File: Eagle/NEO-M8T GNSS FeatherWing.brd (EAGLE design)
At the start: 50.8 x 22.9 mm, 31 parts, among them Q1 DMG3415U-7, Q2 2N2222, SW1 KMR2, U1 NEO-M8, X1 uFL

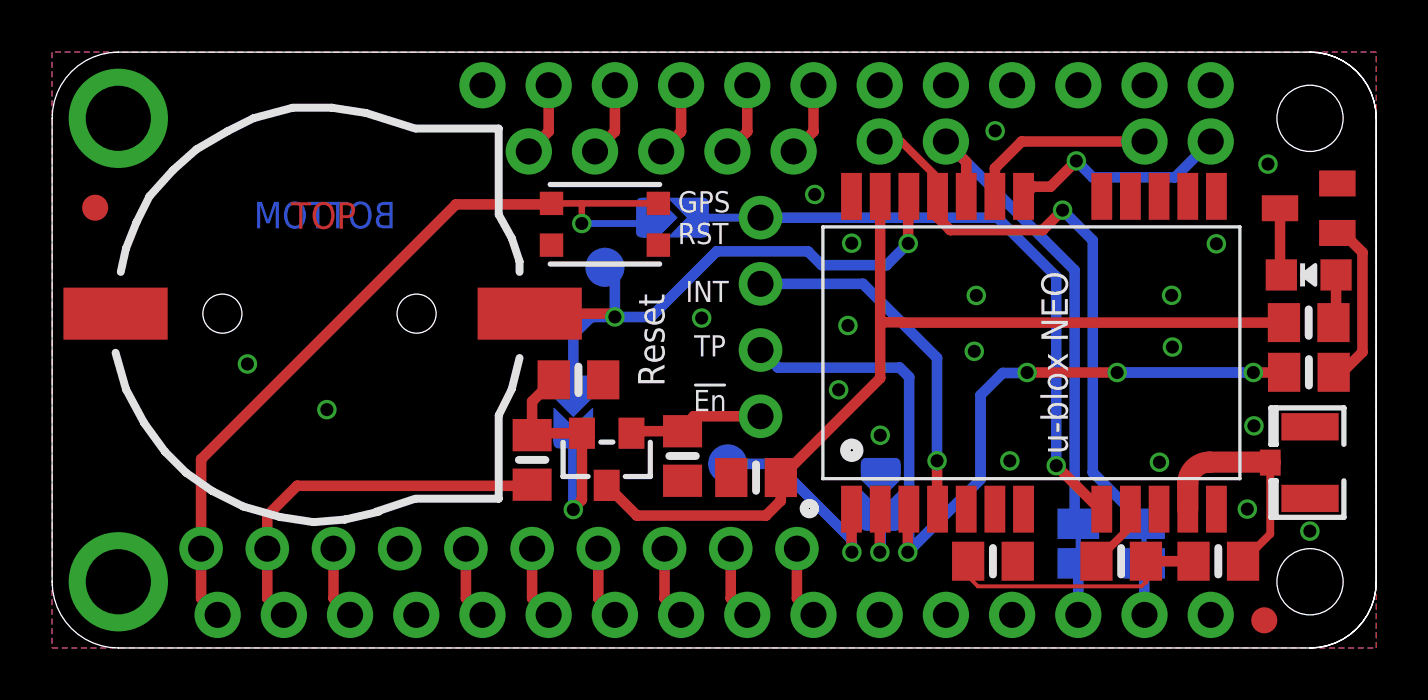
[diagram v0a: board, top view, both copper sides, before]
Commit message: Groundplane improvements
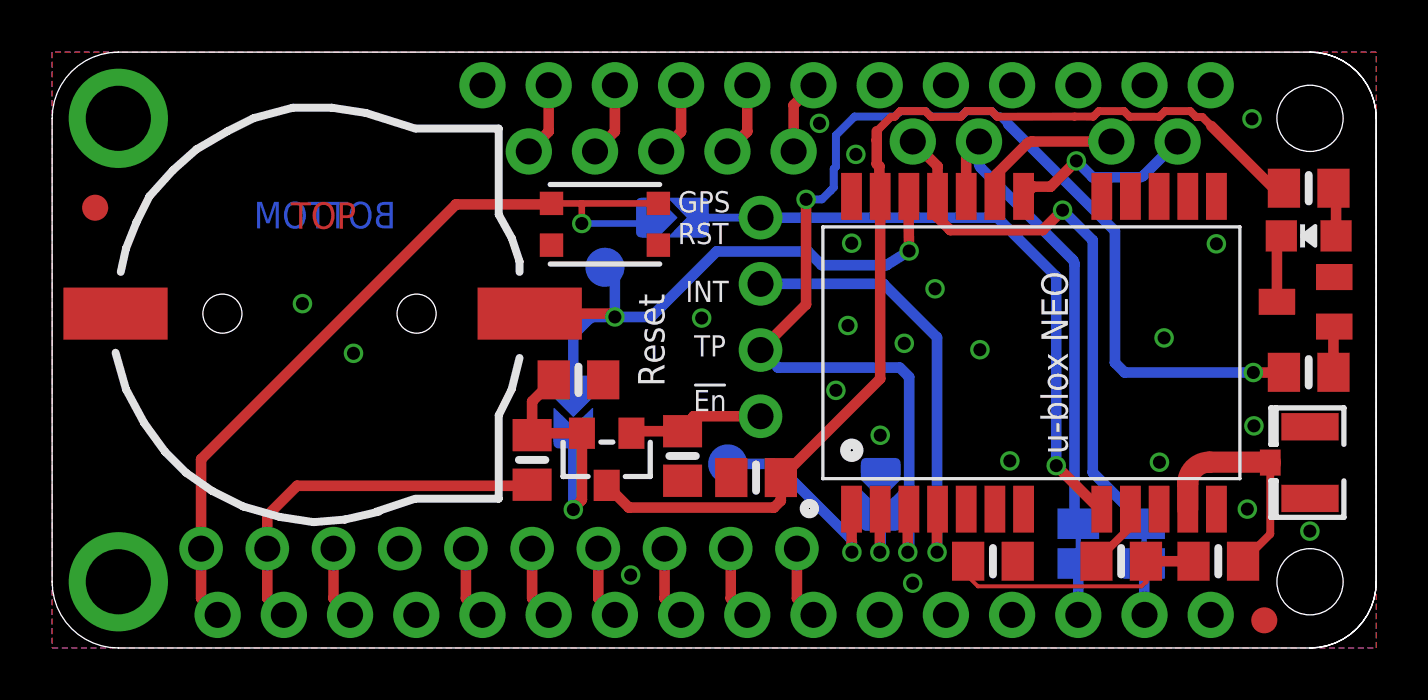
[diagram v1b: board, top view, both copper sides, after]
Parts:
- moved R1 5.16 mm to (48.2, 17.6)
- moved Q2 3.59 mm to (48.1, 13.3)
- moved LED1 1.50 mm to (48.2, 15.8)
- moved JP5 1.27 mm to (41.9, 19.4)
- moved JP3 1.27 mm to (34.3, 19.4)
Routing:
- net TP: track 33.7 -> 49.2 mm, vias 4 -> 3
- net N$19: track 6.52 -> 1.77 mm
- net GPSVCC: track 36.1 -> 40.7 mm
- net EXTINT: track 13.8 -> 17.6 mm
- net SCL: track 7.24 -> 5.77 mm
- net SDA: track 8.57 -> 7.29 mm
- net RX: track 23.0 -> 22.0 mm
- net TX: track 19.2 -> 18.5 mm

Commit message: Added SCL and SDA pullups
Managed to squeeze in pull-up resistors for SCL and SDA.
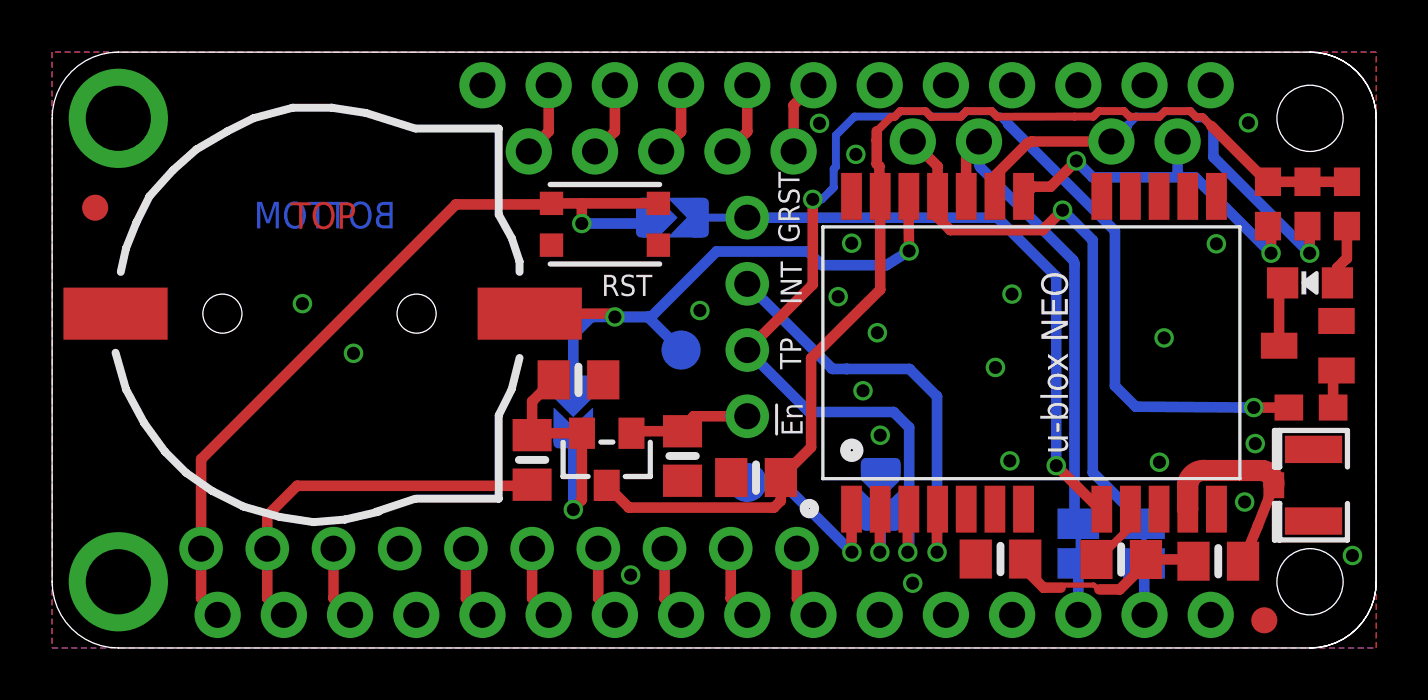
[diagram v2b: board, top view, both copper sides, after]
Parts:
- added R5, R6: 1K, microbuilder:0603-NO
- R1: value 470 ohm -> 470R; device microbuilder:0805-NO -> microbuilder:0603-NO
- R3: device microbuilder:0805-NO -> microbuilder:0603-NO
- moved TP1 4.31 mm to (24.1, 11.4)
- moved LED1 1.80 mm to (48.3, 14.0)
- moved Q2 1.69 mm to (48.2, 11.6)
- moved R1 1.59 mm to (49.7, 17.0), turned to 270 degrees
- moved R3 1.36 mm to (48.3, 9.22)
- moved TP2 1.04 mm to (26.7, 6.35)
- moved X1 0.88 mm to (48.4, 6.24)
- moved JP1 0.51 mm to (26.7, 12.7)
- moved C3 0.30 mm to (36.4, 3.41), turned to 180 degrees
- moved R4 0.07 mm to (41.0, 3.40)
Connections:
- net N$12 renamed RST
- net GPSVCC: now also R1.1, R5.1, R6.1; no longer R1.2
- net N$2: now also R1.2; no longer R1.1
- net SCL: now also R6.2
- net SDA: now also R5.2
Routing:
- net SCL: track 5.77 -> 17.9 mm, vias 0 -> 1
- net SDA: track 7.29 -> 14.1 mm, vias 1 -> 2
- net GPSVCC: track 40.7 -> 43.0 mm
- net N$4: track 10.3 -> 8.01 mm
- net SAFEBOOT: track 8.07 -> 6.77 mm
- net VBACKUP: track 24.0 -> 25.0 mm
- net ANT: track 8.71 -> 7.86 mm
- net N$2: track 1.87 -> 2.71 mm
- net EXTINT: track 17.6 -> 16.8 mm
- net TP: track 49.2 -> 49.9 mm
- net ENABLE: track 5.25 -> 4.75 mm
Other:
- board text added: "GRST"
- board text removed: "GPS RST"
- board text removed: "R1"
- board text removed: "R3"
- board text removed: "Reset"
